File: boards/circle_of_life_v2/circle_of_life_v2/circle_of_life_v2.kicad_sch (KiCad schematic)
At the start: 118 parts, among them IC1 ESP32-WROOM-32E-N8R2, IC2 CP2102C-A01-GQFN28, IC3 TC1262-3.3VDB, IC4 TPS565242DRLR, IC5 LT3922EUFD#PBF, J1 UART Programmer, J2 JTAG Connector, J3 Servo Motor Connector, J4 Power Connector, J5 Water Pump Connector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

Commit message: Added PCB V2
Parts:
- added H1, H2, H3, H4: MountingHole, MountingHole:MountingHole_3.2mm_M3_ISO7380, symbol Mechanical:MountingHole
- C15: footprint Capacitor_SMD:C_0603_1608Metric -> Capacitor_SMD:C_0805_2012Metric_Pad1.18x1.45mm_HandSolder
- C33: footprint SamacSys_Parts:CAPC3216X180N -> Resistor_SMD:R_0805_2012Metric_Pad1.20x1.40mm_HandSolder
- C42: footprint Capacitor_SMD:C_1206_3216Metric -> Capacitor_SMD:C_0805_2012Metric
- C5: footprint Capacitor_SMD:C_0603_1608Metric -> Capacitor_SMD:C_0805_2012Metric

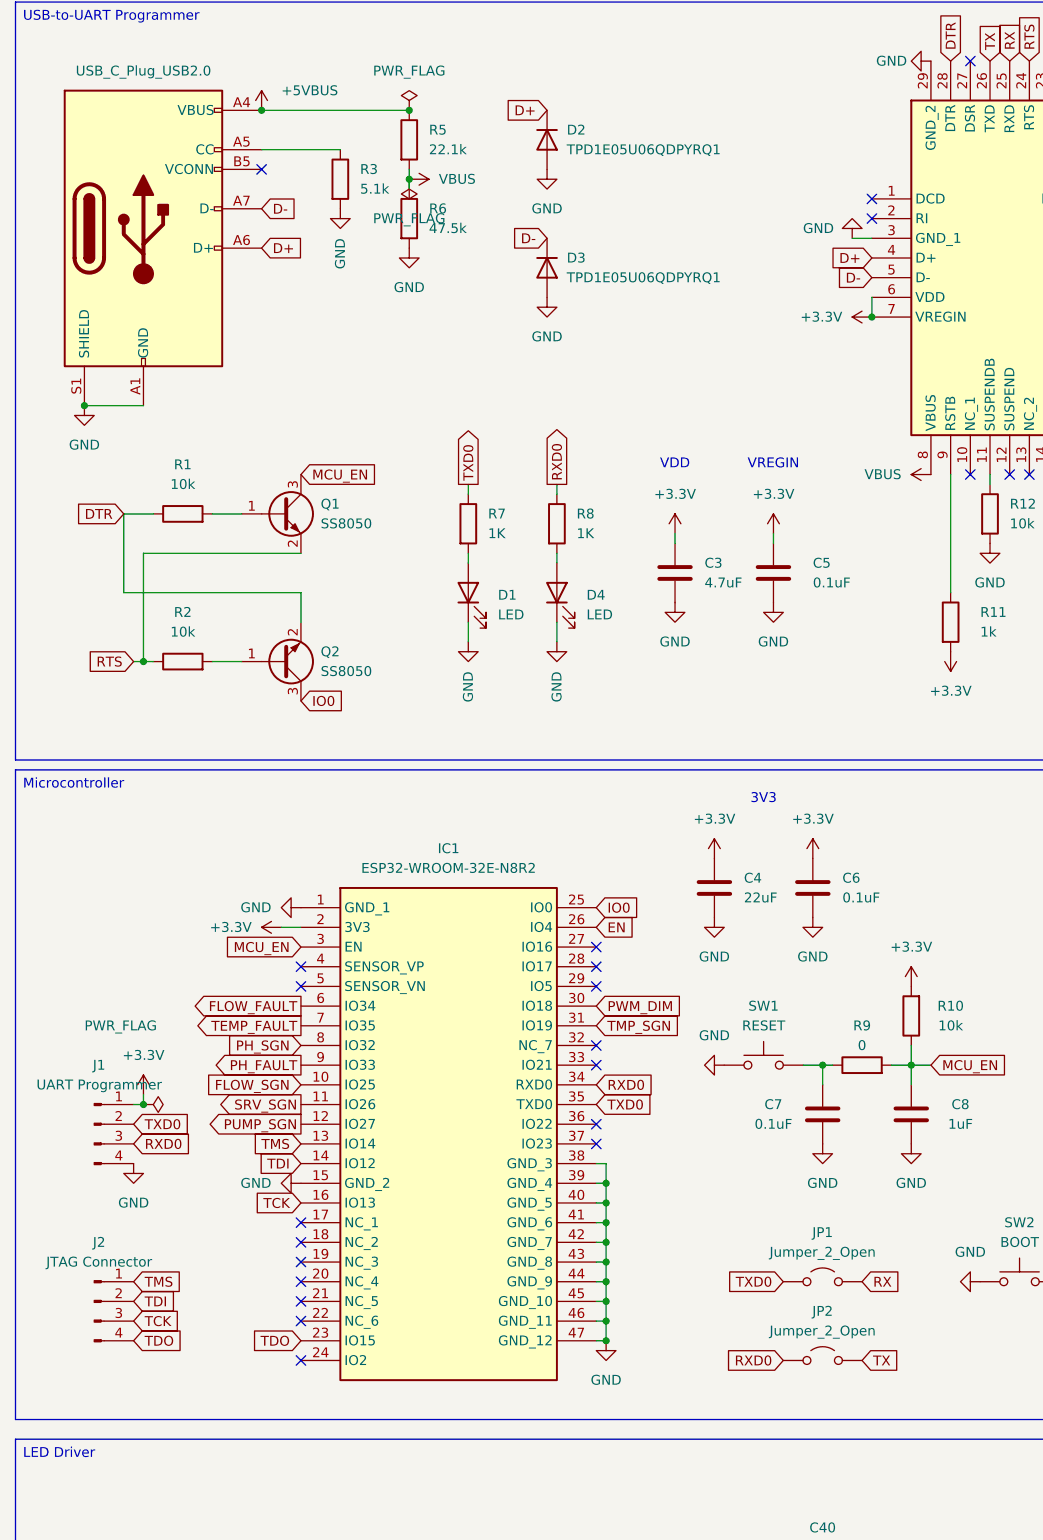
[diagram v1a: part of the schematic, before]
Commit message: Routes fixed and resistors added
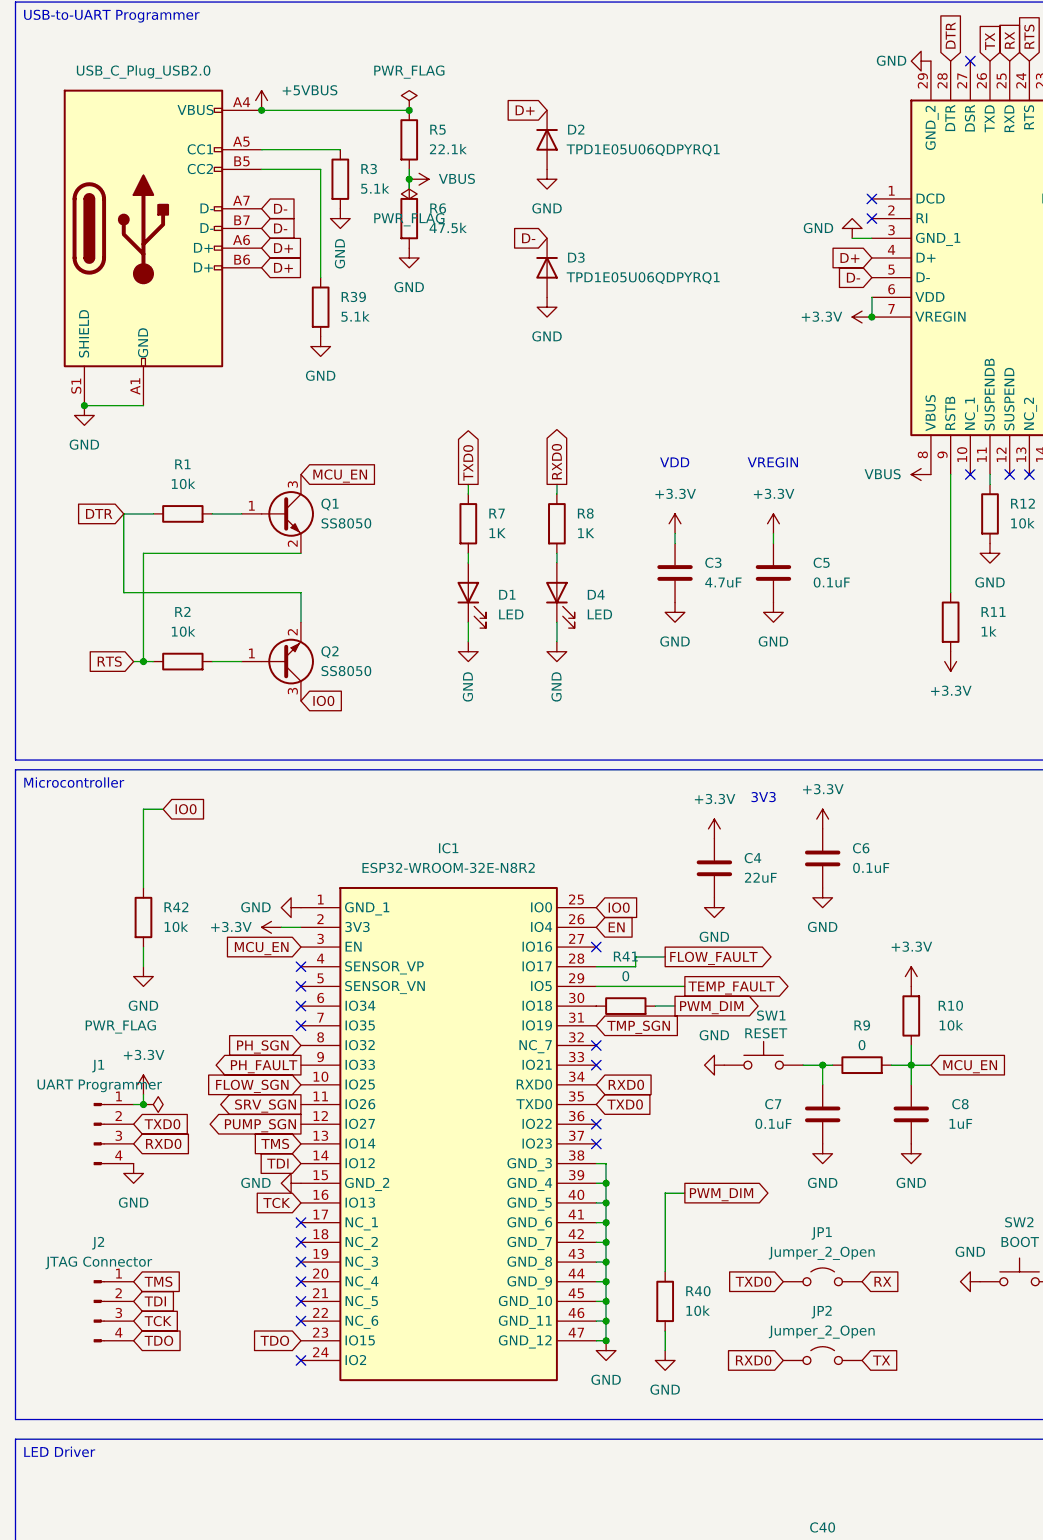
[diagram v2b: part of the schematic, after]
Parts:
- added R39: 5.1k, Resistor_SMD:R_0603_1608Metric, symbol Device:R
- added R40, R42: 10k, SamacSys_Parts:RESC1608X55N, symbol Device:R
- added R41: 0, SamacSys_Parts:RESC1608X55N, symbol Device:R
- P1: symbol Connector:USB_C_Plug_USB2.0 -> Connector:USB_C_Receptacle_USB2.0_14P
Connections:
- net D+: now also P1.B6 (D+)
- net D-: now also P1.B7 (D-)
- net FLOW_FAULT: now also IC1.28 (IO17); no longer IC1.6 (IO34)
- net GND: now also R39.2, R40.2, R42.2
- net IO0: now also R42.1
- net PWM_DIM: now also R40.1, R41.2; no longer IC1.30 (IO18)
- net TEMP_FAULT: now also IC1.29 (IO5); no longer IC1.7 (IO35)
- net at P1.B5 (CC2): now also R39.1
- new net: IC1.30 (IO18), R41.1
- no-connect marks 36 -> 35
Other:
- moved on the sheet: C4, C6

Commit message: Uploaded Estela notebook
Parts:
- removed JP1, JP2: Jumper_2_Open, Jumper:SolderJumper-2_P1.3mm_Open_RoundedPad1.0x1.5mm, symbol Jumper:Jumper_2_Open
- removed R42: 10k, SamacSys_Parts:RESC1608X55N, symbol Device:R
- added NT1, NT2: NetTie_2, NetTie:NetTie-2_SMD_Pad0.5mm, symbol Device:NetTie_2
- added R43: 10k, Resistor_SMD:R_0603_1608Metric, symbol Device:R
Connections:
- net +3.3V: now also R43.2
- net IO0: now also R43.1
- net RX: now also NT1.2
- net RXD0: now also NT2.1
- net TX: now also NT2.2
- net TXD0: now also NT1.1
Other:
- moved on the sheet: R40
